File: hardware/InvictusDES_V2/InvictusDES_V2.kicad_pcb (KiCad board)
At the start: 4 copper layers, 55.5 x 40.9 mm, 70 parts, among them J1 Screw_Terminal_01x02, J10 USB_B_Micro, J11 Conn_01x06, J12 Micro_SD_Card, J2 Conn_02x05_Odd_Even, J3 Conn_01x06, J9 Conn_01x04, U1 TPSM863257RDXR, U2 STM32F405RGTx, U3 TPS2116DRL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

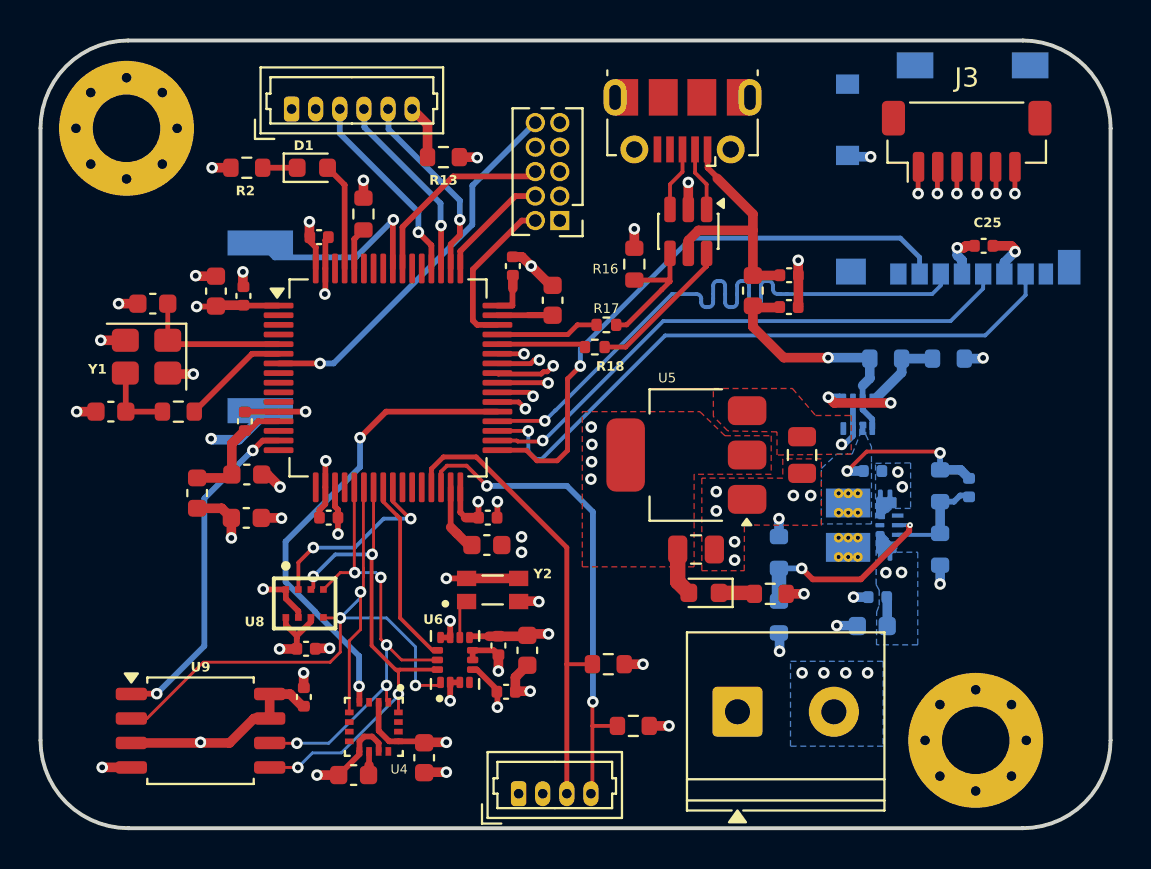
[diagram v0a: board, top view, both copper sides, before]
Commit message: Test Points, spi bus tidying, and fab prep
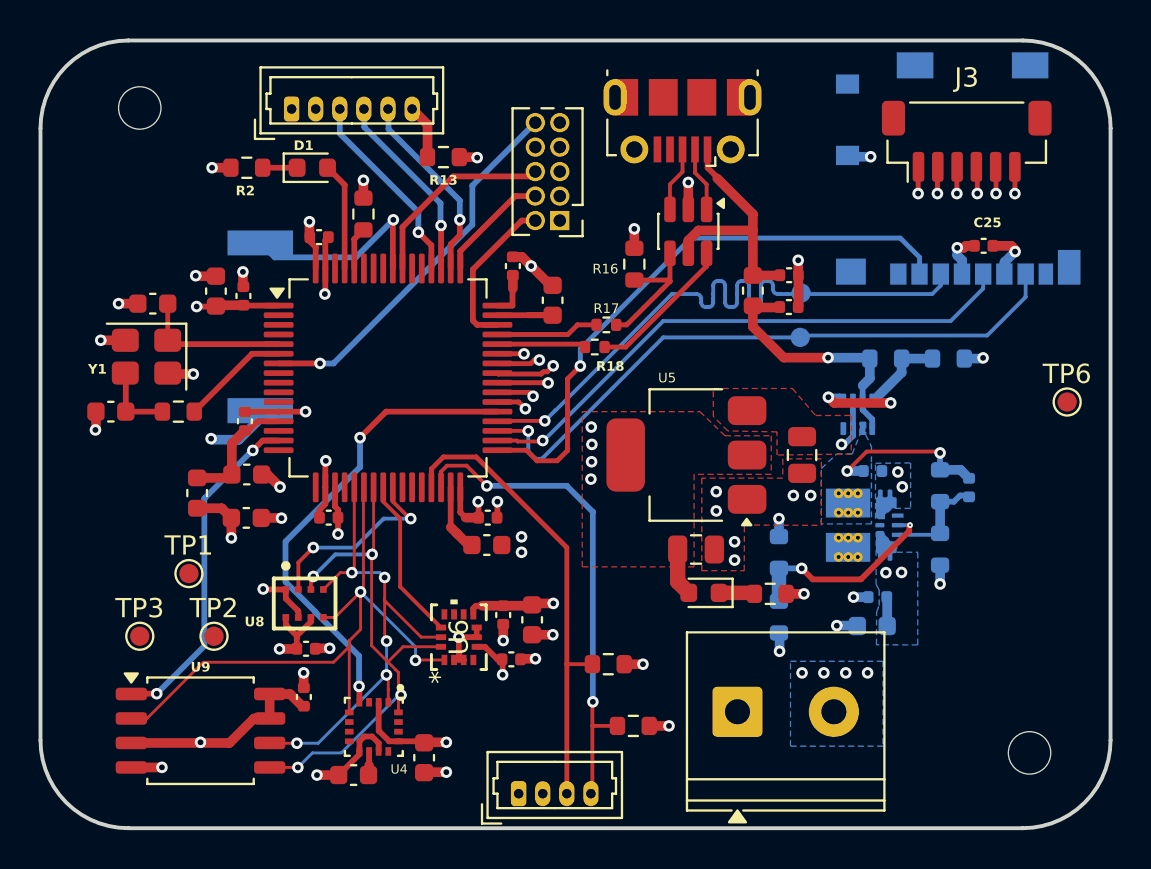
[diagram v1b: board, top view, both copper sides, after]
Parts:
- removed Y2: 32.768Khz, OV-7604-C7_32.768KHZ_20PPM_TA_QC:OSC_OV-7604-C7_32.768KHZ_20PPM_TA_QC
- added TP1: TestPoint, TestPoint:TestPoint_Pad_D1.0mm, F.Cu at (101.0, 114.7)
- added TP2: TestPoint, TestPoint:TestPoint_Pad_D1.0mm, F.Cu at (102.3, 117.9)
- added TP3: TestPoint, TestPoint:TestPoint_Pad_D1.0mm, F.Cu at (98.5, 117.9)
- added TP4: TestPoint, TestPoint:TestPoint_Pad_D1.0mm, B.Cu at (132.8, 100.1)
- added TP5: TestPoint, TestPoint:TestPoint_Pad_D1.0mm, B.Cu at (132.7, 102.4)
- added TP6: TestPoint, TestPoint:TestPoint_Pad_D1.0mm, F.Cu at (146.6, 105.8)
- C21: value 2u2 -> 100n
- C22: value 10n -> 10u
- H1, H4: footprint MountingHole:MountingHole_3.5mm_Pad_Via -> MountingHole:MountingHole_2.2mm_M2
- U6: value ICM-42688-P -> LSM6DSV32XTR; footprint ICM-42688-P (3):PQFN50P300X250X97-14N -> LSM6DSV32XTR:LGA-14L_2p5X3p0X0p86_STM
- moved H4 2.87 mm to (144.6, 124.0)
- moved C22 1.70 mm to (117.7, 119.1)
- moved C18 1.60 mm to (117.3, 116.8)
- moved C21 1.60 mm to (118.8, 117.0)
- moved H1 1.26 mm to (98.5, 90.5)
- moved U6 1.20 mm to (115.0, 117.9)
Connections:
- U1 pad 11: 5V_REG -> (no net)
- U1 pad 12: 5V_REG -> (no net)
- U1 pad 13: 5V_REG -> (no net)
- U1 pad 17: 5V_REG -> (no net)
- U1 pad 18: 5V_REG -> (no net)
- U1 pad 19: 5V_REG -> (no net)
- U6 pad 10: GND -> unconnected-(U6-OCS_AUX-Pad10)
- U6 pad 11: GND -> unconnected-(U6-SDO_AUX-Pad11)
- U6 pad 9: Net-(U6-INT2/FSYNC/CLKIN) -> unconnected-(U6-INT2-Pad9)
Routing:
- net +3V3: track 58.0 -> 54.6 mm, vias 20 -> 19
- net GND: track 66.1 -> 63.0 mm, vias 49 -> 48
- net SPI1_MISO: track 36.6 -> 34.2 mm, vias 3 -> 2
- net Net-(U6-INT2/FSYNC/CLKIN): track 2.02 -> 0.00 mm
- net SPI1_SCK: track 24.8 -> 26.2 mm
- net IMU_CS: track 10.0 -> 8.76 mm
- net SPI1_MOSI: track 27.2 -> 28.1 mm
